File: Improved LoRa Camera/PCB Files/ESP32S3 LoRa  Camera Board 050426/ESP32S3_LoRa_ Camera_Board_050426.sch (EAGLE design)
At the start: 79 parts, among them IC1 ESP32S3_DEVKIT, IC2 INA219, IC3 FM24CL64, IC4 NICERF_SX1262, IC5 NICERF_SX1280, IC6 PCA9536, Q1 SI4459, Q2 IRLML6402, Q3 BC547, SW1 PCB_SLIDE_SWITCH2, SW2A DTS-6, SW2B SMALLSMTSWITCH

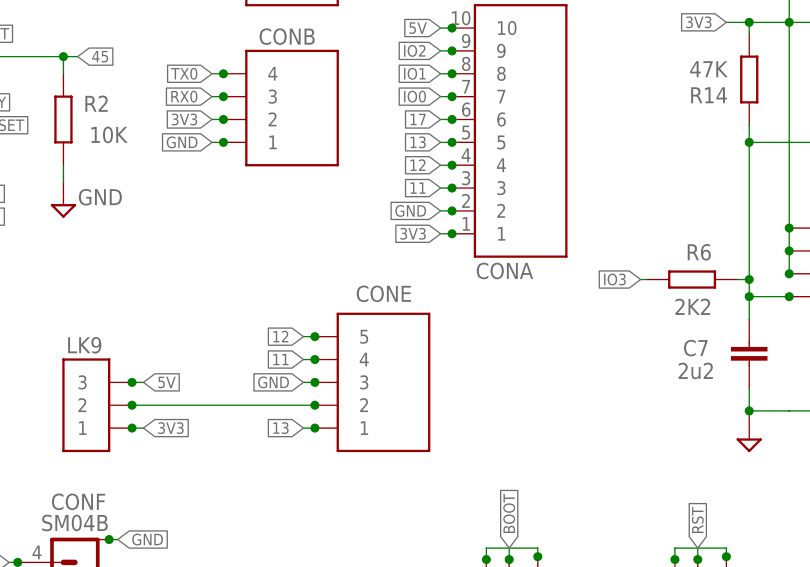
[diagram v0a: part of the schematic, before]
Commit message: Add LR2021
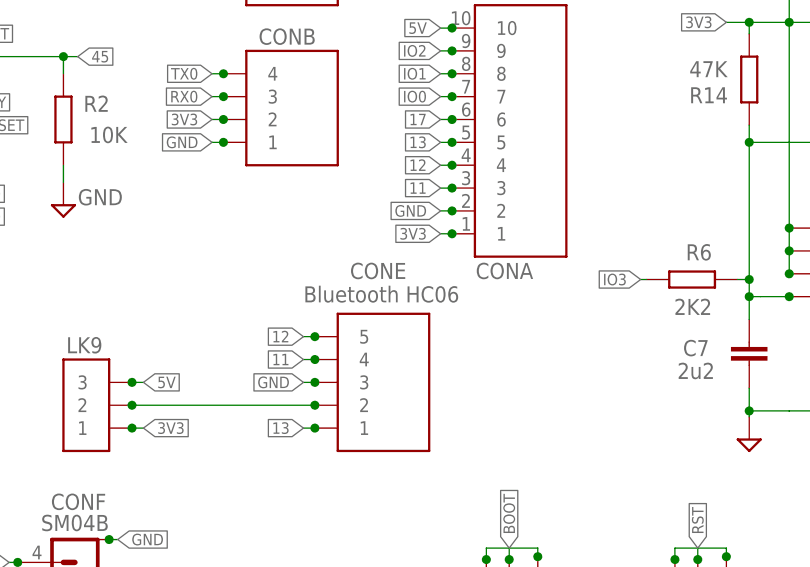
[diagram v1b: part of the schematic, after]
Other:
- note added: "Bluetooth HC06"
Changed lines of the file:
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@@
 <wire x1="104.14" y1="163.195" x2="104.14" y2="197.485" width="0.1524" layer="94" style="longdash"/>
 <text x="105.41" y="193.675" size="2.54" layer="94" font="vector" ratio="15">I2C</text>
+<text x="212.09" y="85.09" size="1.778" layer="95">Bluetooth HC06</text>
 </plain>
 <instances>
@@
 <instance part="CONA" gate="G$1" x="236.22" y="104.14" rot="MR180"/>
 <instance part="CONE" gate="G$1" x="220.98" y="74.93" smashed="yes" rot="MR180">
-<attribute name="NAME" x="217.885" y="86.93" size="1.778" layer="95" rot="MR180"/>
+<attribute name="NAME" x="217.25" y="89.47" size="1.778" layer="95" rot="MR180"/>
 </instance>
 <instance part="CONI" gate="G$1" x="210.82" y="124.46" smashed="yes" rot="MR180">
